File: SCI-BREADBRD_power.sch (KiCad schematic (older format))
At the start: 6 parts, among them P14 CONN_4X2, SW1 DPDT, U1 SN74LVC1G08DBV

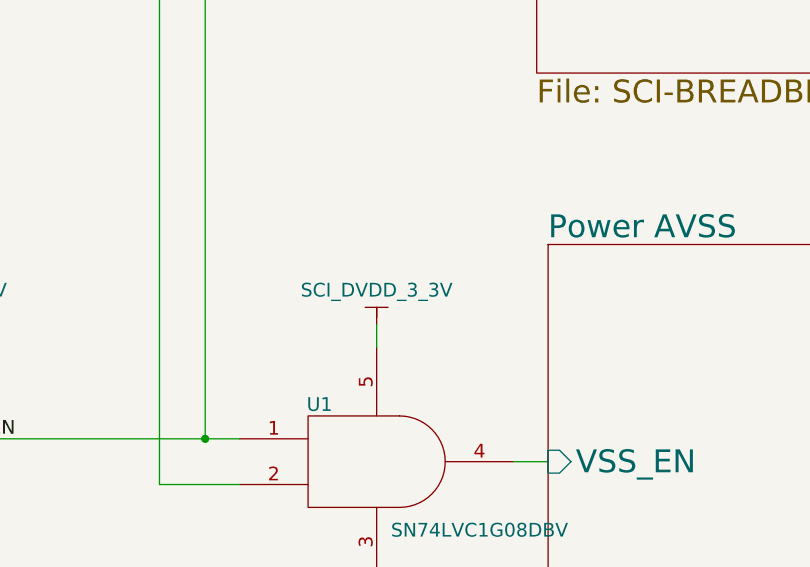
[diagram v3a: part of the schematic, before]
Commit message: Added some bypass caps. Rearranged pins on connectors to make layout easier.
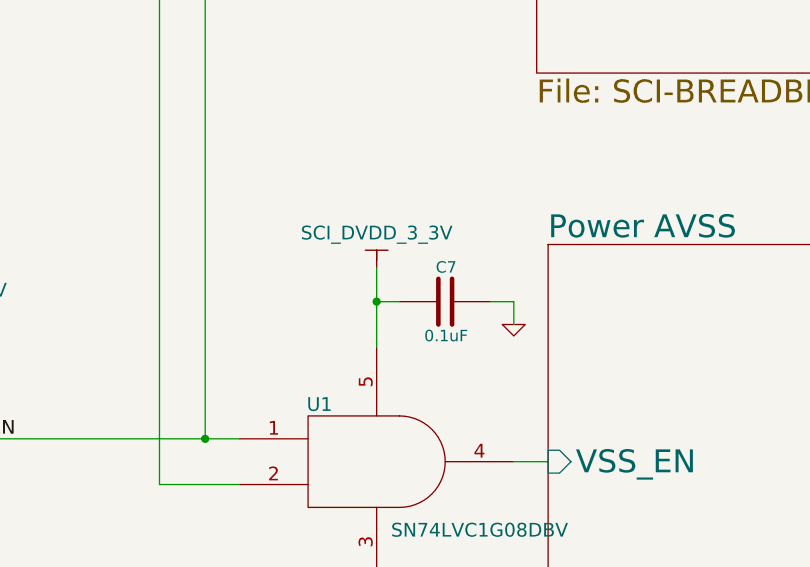
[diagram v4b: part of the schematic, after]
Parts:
- added C7: 0.1uF, 0402, symbol C
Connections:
- net GND: now also C7.2
- net SCI_DVDD_3_3V: now also C7.1
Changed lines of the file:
@@
-EESchema Schematic File Version 2  date Wed 02 May 2012 02:37:03 AM EDT
+EESchema Schematic File Version 2  date Thu 03 May 2012 12:29:14 AM EDT
 LIBS:custom_transistors
 LIBS:TI_custom
@@
 Sheet 6 9
 Title "SCI-BREADBRD-MVK"
-Date "2 may 2012"
+Date "3 may 2012"
 Rev "A"
 Comp "The Ohio State University"
@@
 $EndComp
 $Comp
-L GND #PWR042
+L GND #PWR48
 U 1 1 4F9A1627
 P 2550 4650
-F 0 "#PWR042" H 2550 4650 30  0001 C CNN
+F 0 "#PWR48" H 2550 4650 30  0001 C CNN
 F 1 "GND" H 2550 4580 30  0001 C CNN
 	1    2550 4650
@@
 DUAL_SPLY_EN
 $Comp
-L GND #PWR043
+L GND #PWR54
 U 1 1 4F9A1F73
 P 6750 5600
-F 0 "#PWR043" H 6750 5600 30  0001 C CNN
+F 0 "#PWR54" H 6750 5600 30  0001 C CNN
 F 1 "GND" H 6750 5530 30  0001 C CNN
 	1    6750 5600
@@
 $EndComp
 $Comp
-L GND #PWR044
+L GND #PWR51
 U 1 1 4F9A4A85
 P 4750 5650
-F 0 "#PWR044" H 4750 5650 30  0001 C CNN
+F 0 "#PWR51" H 4750 5650 30  0001 C CNN
 F 1 "GND" H 4750 5580 30  0001 C CNN
 	1    4750 5650
@@
 $EndComp
 $Comp
-L GND #PWR045
+L GND #PWR49
 U 1 1 4F9AB470
 P 3000 2450
-F 0 "#PWR045" H 3000 2450 30  0001 C CNN
+F 0 "#PWR49" H 3000 2450 30  0001 C CNN
 F 1 "GND" H 3000 2380 30  0001 C CNN
 	1    3000 2450
@@
 $EndComp
 $Comp
-L SCI_DVDD_3_3V #PWR046
+L SCI_DVDD_3_3V #PWR50
 U 1 1 4F9AED7C
 P 3100 1050
-F 0 "#PWR046" H 3100 1150 30  0001 C CNN
+F 0 "#PWR50" H 3100 1150 30  0001 C CNN
 F 1 "SCI_DVDD_3_3V" H 3100 1200 60  0000 C CNN
 	1    3100 1050
@@
 $EndComp
 $Comp
-L SCI_DVDD_3_3V #PWR047
+L SCI_DVDD_3_3V #PWR52
 U 1 1 4F9AEECF
 P 4800 4400
-F 0 "#PWR047" H 4800 4500 30  0001 C CNN
+F 0 "#PWR52" H 4800 4500 30  0001 C CNN
 F 1 "SCI_DVDD_3_3V" H 4800 4550 60  0000 C CNN
 	1    4800 4400
@@
 $EndComp
 $Comp
-L SCI_DVDD_3_3V #PWR048
+L SCI_DVDD_3_3V #PWR53
 U 1 1 4F9AEF3E
-P 6750 4400
-F 0 "#PWR048" H 6750 4500 30  0001 C CNN
-F 1 "SCI_DVDD_3_3V" H 6750 4550 60  0000 C CNN
-	1    6750 4400
-	1    0    0    -1
-$EndComp
-$Comp
-L AFE/SCI_ANLG_VSS #PWR049
+P 6750 4150
+F 0 "#PWR53" H 6750 4250 30  0001 C CNN
+F 1 "SCI_DVDD_3_3V" H 6750 4300 60  0000 C CNN
+	1    6750 4150
+	1    0    0    -1
+$EndComp
+$Comp
+L AFE/SCI_ANLG_VSS #PWR46
 U 1 1 4FA0D213
 P 1850 5350
-F 0 "#PWR049" H 1850 5250 30  0001 C CNN
+F 0 "#PWR46" H 1850 5250 30  0001 C CNN
 F 1 "AFE/SCI_ANLG_VSS" H 1850 5200 60  0000 C CNN
 	1    1850 5350
@@
 $EndComp
 $Comp
-L AFE/SCI_ANLG_VDD #PWR050
+L AFE/SCI_ANLG_VDD #PWR47
 U 1 1 4FA0E56B
 P 1850 5950
-F 0 "#PWR050" H 1850 6050 30  0001 C CNN
+F 0 "#PWR47" H 1850 6050 30  0001 C CNN
 F 1 "AFE/SCI_ANLG_VDD" H 1850 6050 60  0000 C CNN
 	1    1850 5950
 	1    0    0    -1
 $EndComp
+$Comp
+L C C7
+U 1 1 4FA20BB3
+P 7050 4300
+F 0 "C7" V 7200 4250 50  0000 L CNN
+F 1 "0.1uF" V 6900 4200 50  0000 L CNN
+F 2 "0402" H 7050 4300 60  0001 C CNN
+F 4 "Taiyo Yuden" H 7050 4300 60  0001 C CNN "Manufacturer"
+F 5 "LMK105BJ104KV-F" H 7050 4300 60  0001 C CNN "Part Number"
+F 6 "CAP CER 0.1UF 10V 10% X5R 0402" H 7050 4300 60  0001 C CNN "Description"
+	1    7050 4300
+	0    -1   -1   0
+$EndComp
+$Comp
+L GND #PWR55
+U 1 1 4FA20BB9
+P 7350 4400
+F 0 "#PWR55" H 7350 4400 30  0001 C CNN
+F 1 "GND" H 7350 4330 30  0001 C CNN
+	1    7350 4400
+	1    0    0    -1
+$EndComp
 Wire Wire Line
 	2750 4700 2750 5300
@@
 	4800 4700 4800 4400
 Wire Wire Line
-	6750 4400 6750 4500
+	6750 4150 6750 4500
 Wire Wire Line
 	6750 5500 6750 5600
@@
 	2450 6100 2450 6200
 Connection ~ 2450 6200
+Wire Wire Line
+	7350 4300 7350 4400
+Wire Wire Line
+	7250 4300 7350 4300
+Wire Wire Line
+	6850 4300 6750 4300
+Connection ~ 6750 4300
 $EndSCHEMATC

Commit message: More layout progress
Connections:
- net MOD_VSS: now reaches P14.6, P14.8, SW1.2
- net Power AVDD/AVDD renamed MOD_VDD
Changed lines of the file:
@@
-EESchema Schematic File Version 2  date Thu 03 May 2012 12:29:14 AM EDT
+EESchema Schematic File Version 2  date Fri 04 May 2012 05:17:17 PM EDT
 LIBS:custom_transistors
 LIBS:TI_custom
@@
 Sheet 6 9
 Title "SCI-BREADBRD-MVK"
-Date "3 may 2012"
+Date "4 may 2012"
 Rev "A"
 Comp "The Ohio State University"
@@
 $EndComp
 $Comp
-L GND #PWR48
+L GND #PWR048
 U 1 1 4F9A1627
-P 2550 4650
-F 0 "#PWR48" H 2550 4650 30  0001 C CNN
-F 1 "GND" H 2550 4580 30  0001 C CNN
-	1    2550 4650
-	1    0    0    -1
+P 3450 4500
+F 0 "#PWR048" H 3450 4500 30  0001 C CNN
+F 1 "GND" H 3450 4430 30  0001 C CNN
+	1    3450 4500
+	0    1    1    0
 $EndComp
 NoConn ~ 4500 4500
@@
 DUAL_SPLY_EN
 $Comp
-L GND #PWR54
+L GND #PWR049
 U 1 1 4F9A1F73
 P 6750 5600
-F 0 "#PWR54" H 6750 5600 30  0001 C CNN
+F 0 "#PWR049" H 6750 5600 30  0001 C CNN
 F 1 "GND" H 6750 5530 30  0001 C CNN
 	1    6750 5600
@@
 $EndComp
 $Comp
-L GND #PWR51
+L GND #PWR050
 U 1 1 4F9A4A85
 P 4750 5650
-F 0 "#PWR51" H 4750 5650 30  0001 C CNN
+F 0 "#PWR050" H 4750 5650 30  0001 C CNN
 F 1 "GND" H 4750 5580 30  0001 C CNN
 	1    4750 5650
@@
 $EndComp
 $Comp
-L GND #PWR49
+L GND #PWR051
 U 1 1 4F9AB470
 P 3000 2450
-F 0 "#PWR49" H 3000 2450 30  0001 C CNN
+F 0 "#PWR051" H 3000 2450 30  0001 C CNN
 F 1 "GND" H 3000 2380 30  0001 C CNN
 	1    3000 2450
@@
 $EndComp
 $Comp
-L SCI_DVDD_3_3V #PWR50
+L SCI_DVDD_3_3V #PWR052
 U 1 1 4F9AED7C
 P 3100 1050
-F 0 "#PWR50" H 3100 1150 30  0001 C CNN
+F 0 "#PWR052" H 3100 1150 30  0001 C CNN
 F 1 "SCI_DVDD_3_3V" H 3100 1200 60  0000 C CNN
 	1    3100 1050
@@
 $EndComp
 $Comp
-L SCI_DVDD_3_3V #PWR52
+L SCI_DVDD_3_3V #PWR053
 U 1 1 4F9AEECF
 P 4800 4400
-F 0 "#PWR52" H 4800 4500 30  0001 C CNN
+F 0 "#PWR053" H 4800 4500 30  0001 C CNN
 F 1 "SCI_DVDD_3_3V" H 4800 4550 60  0000 C CNN
 	1    4800 4400
@@
 $EndComp
 $Comp
-L SCI_DVDD_3_3V #PWR53
+L SCI_DVDD_3_3V #PWR054
 U 1 1 4F9AEF3E
 P 6750 4150
-F 0 "#PWR53" H 6750 4250 30  0001 C CNN
+F 0 "#PWR054" H 6750 4250 30  0001 C CNN
 F 1 "SCI_DVDD_3_3V" H 6750 4300 60  0000 C CNN
 	1    6750 4150
@@
 $EndComp
 $Comp
-L AFE/SCI_ANLG_VSS #PWR46
+L AFE/SCI_ANLG_VSS #PWR055
 U 1 1 4FA0D213
 P 1850 5350
-F 0 "#PWR46" H 1850 5250 30  0001 C CNN
+F 0 "#PWR055" H 1850 5250 30  0001 C CNN
 F 1 "AFE/SCI_ANLG_VSS" H 1850 5200 60  0000 C CNN
 	1    1850 5350
@@
 $EndComp
 $Comp
-L AFE/SCI_ANLG_VDD #PWR47
+L AFE/SCI_ANLG_VDD #PWR056
 U 1 1 4FA0E56B
 P 1850 5950
-F 0 "#PWR47" H 1850 6050 30  0001 C CNN
+F 0 "#PWR056" H 1850 6050 30  0001 C CNN
 F 1 "AFE/SCI_ANLG_VDD" H 1850 6050 60  0000 C CNN
 	1    1850 5950
@@
 $EndComp
 $Comp
-L GND #PWR55
+L GND #PWR057
 U 1 1 4FA20BB9
 P 7350 4400
-F 0 "#PWR55" H 7350 4400 30  0001 C CNN
+F 0 "#PWR057" H 7350 4400 30  0001 C CNN
 F 1 "GND" H 7350 4330 30  0001 C CNN
 	1    7350 4400
 	1    0    0    -1
 $EndComp
+$Comp
+L MOD_VDD #PWR?
+U 1 1 4FA44BD2
+P 2300 6550
+F 0 "#PWR?" H 2300 6650 30  0001 C CNN
+F 1 "MOD_VDD" H 2300 6700 60  0000 C CNN
+	1    2300 6550
+	1    0    0    -1
+$EndComp
+$Comp
+L MOD_VSS #PWR?
+U 1 1 4FA44BFF
+P 2450 4800
+F 0 "#PWR?" H 2450 4700 30  0001 C CNN
+F 1 "MOD_VSS" H 2450 4650 60  0000 C CNN
+	1    2450 4800
+	1    0    0    -1
+$EndComp
 Wire Wire Line
 	2750 4700 2750 5300
 Wire Wire Line
-	2750 4700 3600 4700
-Wire Wire Line
-	2550 4650 2550 4500
-Wire Wire Line
-	2550 4500 3600 4500
+	2450 4700 3600 4700
+Wire Wire Line
+	3450 4500 3600 4500
 Wire Wire Line
 	3600 4900 3450 4900
@@
 	2650 6200 2650 6100
 Wire Wire Line
-	2750 6100 2750 6350
+	2750 6100 2750 6650
 Connection ~ 2650 6200
 Connection ~ 2750 6200
@@
 	6850 4300 6750 4300
 Connection ~ 6750 4300
+Wire Wire Line
+	2450 4700 2450 4800
+Connection ~ 2750 4700
+Wire Wire Line
+	2750 6650 2300 6650
+Wire Wire Line
+	2300 6650 2300 6550
+Connection ~ 2750 6350
 $EndSCHEMATC

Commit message: Finished initial PCB layout
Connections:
- net AFE/SCI_ANLG_VDD: now also P14.2; no longer P14.3
- net AFE/SCI_ANLG_VSS: now also P14.3; no longer P14.2
- net MOD_VDD: now also P14.6; no longer P14.7
- net MOD_VSS: now also P14.7; no longer P14.6
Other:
- moved on the sheet: P14
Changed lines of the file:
@@
-EESchema Schematic File Version 2  date Fri 04 May 2012 05:17:17 PM EDT
+EESchema Schematic File Version 2  date Tue 08 May 2012 11:34:32 AM EDT
 LIBS:custom_transistors
 LIBS:TI_custom
@@
 Sheet 6 9
 Title "SCI-BREADBRD-MVK"
-Date "4 may 2012"
+Date "7 may 2012"
 Rev "A"
 Comp "The Ohio State University"
@@
 $EndComp
 $Comp
-L AFE/SCI_ANLG_VSS #PWR055
-U 1 1 4FA0D213
-P 1850 5350
-F 0 "#PWR055" H 1850 5250 30  0001 C CNN
-F 1 "AFE/SCI_ANLG_VSS" H 1850 5200 60  0000 C CNN
-	1    1850 5350
-	1    0    0    -1
-$EndComp
-$Comp
 L CONN_4X2 P14
 U 1 1 4FA0D66E
-P 2600 5700
-F 0 "P14" H 2600 5950 50  0000 C CNN
-F 1 "CONN_4X2" H 2600 5450 40  0000 C CNN
-F 2 "pin_array_4x2" H 2600 5700 60  0001 C CNN
-F 4 "TE Connectivity" H 2600 5700 60  0001 C CNN "Manufacturer"
-F 5 "5-534206-4" H 2600 5700 60  0001 C CNN "Part Number"
-F 6 "SOCKET 2x4POS 0.1in" H 2600 5700 60  0001 C CNN "Description"
-	1    2600 5700
+P 2100 6100
+F 0 "P14" H 2100 6350 50  0000 C CNN
+F 1 "CONN_4X2" H 2100 5850 40  0000 C CNN
+F 2 "pin_array_4x2" H 2100 6100 60  0001 C CNN
+F 4 "TE Connectivity" H 2100 6100 60  0001 C CNN "Manufacturer"
+F 5 "5-534206-4" H 2100 6100 60  0001 C CNN "Part Number"
+F 6 "SOCKET 2x4POS 0.1in" H 2100 6100 60  0001 C CNN "Description"
+	1    2100 6100
 	0    -1   -1   0
-$EndComp
-$Comp
-L AFE/SCI_ANLG_VDD #PWR056
-U 1 1 4FA0E56B
-P 1850 5950
-F 0 "#PWR056" H 1850 6050 30  0001 C CNN
-F 1 "AFE/SCI_ANLG_VDD" H 1850 6050 60  0000 C CNN
-	1    1850 5950
-	1    0    0    -1
 $EndComp
 $Comp
@@
 $EndComp
 $Comp
-L GND #PWR057
+L GND #PWR055
 U 1 1 4FA20BB9
 P 7350 4400
-F 0 "#PWR057" H 7350 4400 30  0001 C CNN
+F 0 "#PWR055" H 7350 4400 30  0001 C CNN
 F 1 "GND" H 7350 4330 30  0001 C CNN
 	1    7350 4400
@@
 $EndComp
 $Comp
-L MOD_VDD #PWR?
+L MOD_VDD #PWR056
 U 1 1 4FA44BD2
-P 2300 6550
-F 0 "#PWR?" H 2300 6650 30  0001 C CNN
-F 1 "MOD_VDD" H 2300 6700 60  0000 C CNN
-	1    2300 6550
-	1    0    0    -1
-$EndComp
-$Comp
-L MOD_VSS #PWR?
+P 10300 2100
+F 0 "#PWR056" H 10300 2200 30  0001 C CNN
+F 1 "MOD_VDD" H 10300 2250 60  0000 C CNN
+	1    10300 2100
+	1    0    0    -1
+$EndComp
+$Comp
+L MOD_VSS #PWR057
 U 1 1 4FA44BFF
-P 2450 4800
-F 0 "#PWR?" H 2450 4700 30  0001 C CNN
-F 1 "MOD_VSS" H 2450 4650 60  0000 C CNN
-	1    2450 4800
-	1    0    0    -1
-$EndComp
-Wire Wire Line
-	2750 4700 2750 5300
-Wire Wire Line
-	2450 4700 3600 4700
+P 3100 4800
+F 0 "#PWR057" H 3100 4700 30  0001 C CNN
+F 1 "MOD_VSS" H 3100 4650 60  0000 C CNN
+	1    3100 4800
+	1    0    0    -1
+$EndComp
+$Comp
+L AFE/SCI_ANLG_VDD #PWR058
+U 1 1 4FA82EB2
+P 1300 5050
+F 0 "#PWR058" H 1300 5150 30  0001 C CNN
+F 1 "AFE/SCI_ANLG_VDD" H 1300 5200 60  0000 C CNN
+	1    1300 5050
+	1    0    0    -1
+$EndComp
+$Comp
+L AFE/SCI_ANLG_VSS #PWR059
+U 1 1 4FA83039
+P 1850 5150
+F 0 "#PWR059" H 1850 5050 30  0001 C CNN
+F 1 "AFE/SCI_ANLG_VSS" H 1850 5000 60  0000 C CNN
+	1    1850 5150
+	-1   0    0    1
+$EndComp
+$Comp
+L MOD_VDD #PWR060
+U 1 1 4FA83150
+P 2200 5300
+F 0 "#PWR060" H 2200 5400 30  0001 C CNN
+F 1 "MOD_VDD" H 2200 5450 60  0000 C CNN
+	1    2200 5300
+	1    0    0    -1
+$EndComp
+$Comp
+L MOD_VSS #PWR061
+U 1 1 4FA83219
+P 2600 5400
+F 0 "#PWR061" H 2600 5300 30  0001 C CNN
+F 1 "MOD_VSS" H 2600 5250 60  0000 C CNN
+	1    2600 5400
+	-1   0    0    1
+$EndComp
+Wire Wire Line
+	3100 4700 3600 4700
 Wire Wire Line
 	3450 4500 3600 4500
@@
 	9700 2400 10300 2400
 Wire Wire Line
-	10300 2400 10300 6350
-Wire Wire Line
-	2650 6200 2750 6200
-Wire Wire Line
-	2650 6200 2650 6100
-Wire Wire Line
-	2750 6100 2750 6650
-Connection ~ 2650 6200
-Connection ~ 2750 6200
-Wire Wire Line
-	2750 6350 10300 6350
-Wire Wire Line
-	2750 5200 2650 5200
-Wire Wire Line
-	2650 5200 2650 5300
-Connection ~ 2650 5200
-Connection ~ 2750 5200
-Wire Wire Line
-	1850 5350 1850 5200
-Wire Wire Line
-	1850 5200 2550 5200
-Wire Wire Line
-	2550 5200 2550 5300
-Wire Wire Line
-	2450 5300 2450 5200
-Connection ~ 2450 5200
-Wire Wire Line
-	1850 5950 1850 6200
-Wire Wire Line
-	1850 6200 2550 6200
-Wire Wire Line
-	2550 6200 2550 6100
-Wire Wire Line
-	2450 6100 2450 6200
-Connection ~ 2450 6200
-Wire Wire Line
 	7350 4300 7350 4400
 Wire Wire Line
@@
 Connection ~ 6750 4300
 Wire Wire Line
-	2450 4700 2450 4800
-Connection ~ 2750 4700
-Wire Wire Line
-	2750 6650 2300 6650
-Wire Wire Line
-	2300 6650 2300 6550
-Connection ~ 2750 6350
+	3100 4700 3100 4800
+Wire Wire Line
+	10300 2400 10300 2100
+Wire Wire Line
+	1300 5050 1300 5650
+Wire Wire Line
+	1300 5650 1950 5650
+Wire Wire Line
+	1950 5650 1950 5700
+Wire Wire Line
+	1850 5150 1850 5600
+Wire Wire Line
+	1850 5600 2050 5600
+Wire Wire Line
+	2050 5600 2050 5700
+Wire Wire Line
+	2200 5300 2200 5550
+Wire Wire Line
+	2200 5550 2150 5550
+Wire Wire Line
+	2150 5550 2150 5700
+Wire Wire Line
+	2600 5400 2250 5400
+Wire Wire Line
+	2250 5400 2250 5700
+$Comp
+L AFE/SCI_ANLG_VDD #PWR062
+U 1 1 4FA833EE
+P 1300 7150
+F 0 "#PWR062" H 1300 7250 30  0001 C CNN
+F 1 "AFE/SCI_ANLG_VDD" H 1300 7300 60  0000 C CNN
+	1    1300 7150
+	1    0    0    1
+$EndComp
+$Comp
+L AFE/SCI_ANLG_VSS #PWR063
+U 1 1 4FA833F4
+P 1850 7050
+F 0 "#PWR063" H 1850 6950 30  0001 C CNN
+F 1 "AFE/SCI_ANLG_VSS" H 1850 6900 60  0000 C CNN
+	1    1850 7050
+	-1   0    0    -1
+$EndComp
+$Comp
+L MOD_VDD #PWR064
+U 1 1 4FA833FA
+P 2200 6900
+F 0 "#PWR064" H 2200 7000 30  0001 C CNN
+F 1 "MOD_VDD" H 2200 7050 60  0000 C CNN
+	1    2200 6900
+	1    0    0    1
+$EndComp
+$Comp
+L MOD_VSS #PWR065
+U 1 1 4FA83400
+P 2600 6800
+F 0 "#PWR065" H 2600 6700 30  0001 C CNN
+F 1 "MOD_VSS" H 2600 6650 60  0000 C CNN
+	1    2600 6800
+	-1   0    0    -1
+$EndComp
+Wire Wire Line
+	1300 7150 1300 6550
+Wire Wire Line
+	1300 6550 1950 6550
+Wire Wire Line
+	1950 6550 1950 6500
+Wire Wire Line
+	1850 7050 1850 6600
+Wire Wire Line
+	1850 6600 2050 6600
+Wire Wire Line
+	2050 6600 2050 6500
+Wire Wire Line
+	2200 6900 2200 6650
+Wire Wire Line
+	2200 6650 2150 6650
+Wire Wire Line
+	2150 6650 2150 6500
+Wire Wire Line
+	2600 6800 2250 6800
+Wire Wire Line
+	2250 6800 2250 6500
 $EndSCHEMATC
